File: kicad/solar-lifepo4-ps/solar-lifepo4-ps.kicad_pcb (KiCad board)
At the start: 2 copper layers, 94 x 75 mm, 56 parts, among them J1 Screw_Terminal_01x02, J2 Screw_Terminal_01x02, J3 Screw_Terminal_01x02, J4 disable-Jumper, J5 SenseVBAT, J6 SenseVSOLAR, T1 SI4435DY, T2 AO3400A, T3 AO3400A, U1 CN3722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

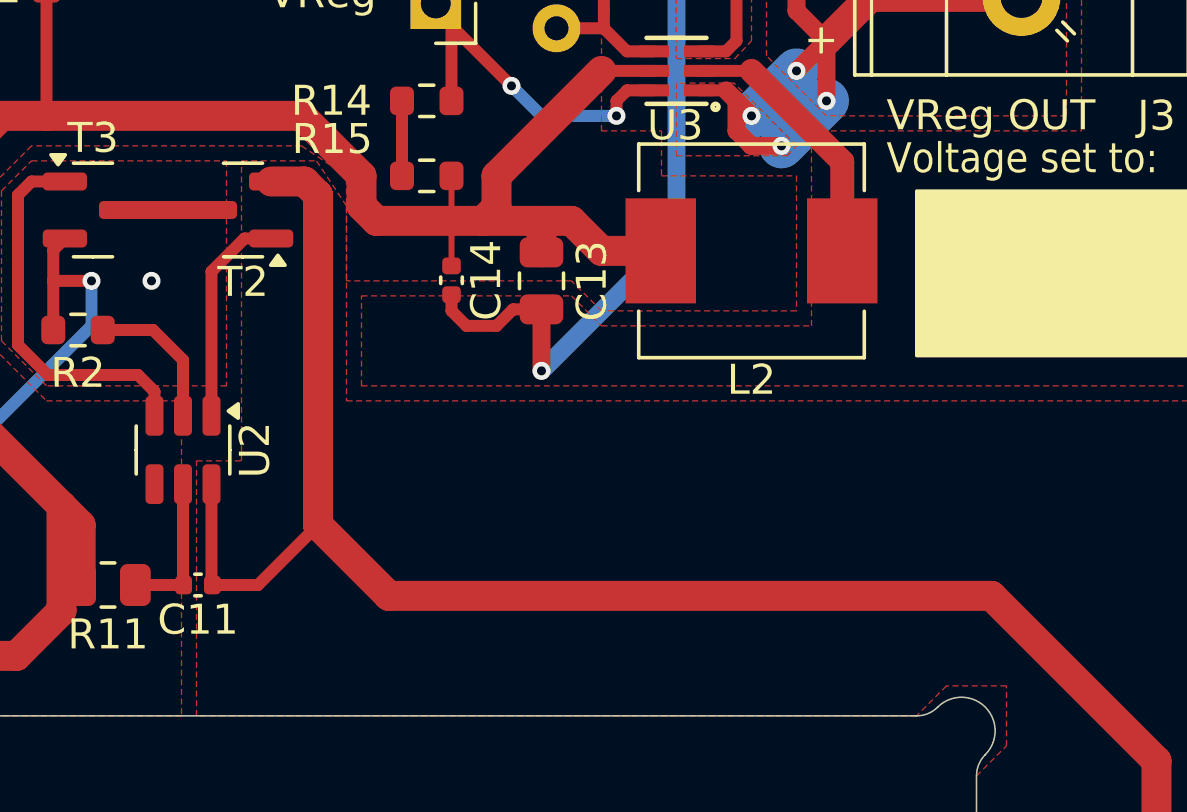
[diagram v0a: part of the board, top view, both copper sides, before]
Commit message: add pushbutton to force the battery protection circuit into "normal" mode. When a battery is inserted, but there is not and has never been enough power to actually charge, the battery protection circuit may remain in a state where the output is turned off. Shorting pins 2+6 (by pressing this button) forces the battery protection IC back into "normal" mode, with output on.
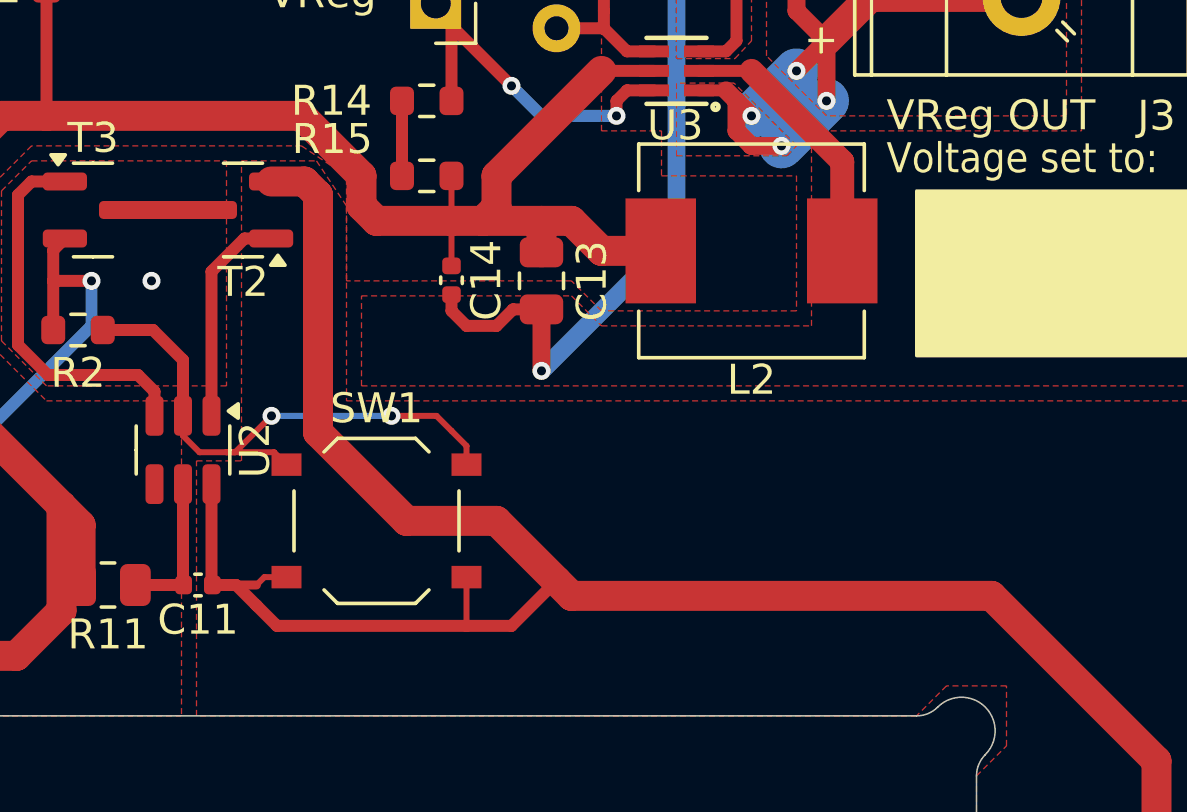
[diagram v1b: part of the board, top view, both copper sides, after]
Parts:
- added SW1: force-normal, Button_Switch_SMD:SW_Push_1P1T_XKB_TS-1187A, F.Cu at (106.5, 90.5)
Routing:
- net Net-(U2-CS): track 4.95 -> 19.0 mm, vias 0 -> 2
- net VBAT-: track 66.4 -> 76.3 mm

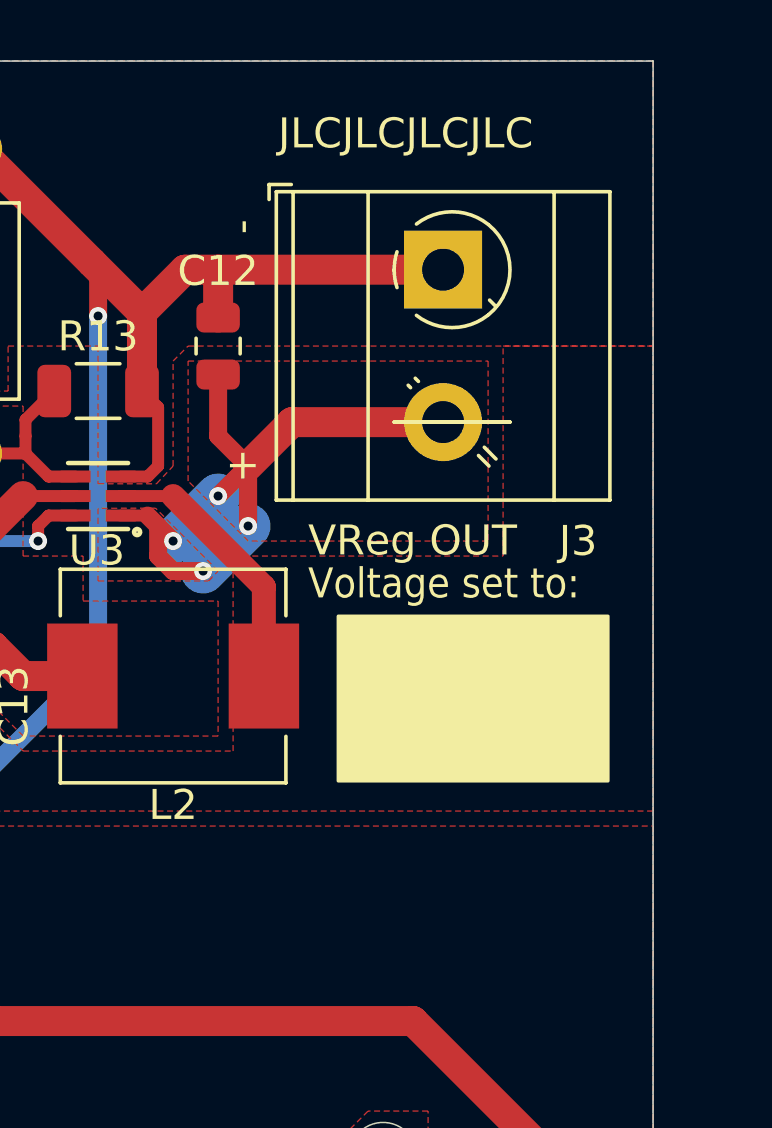
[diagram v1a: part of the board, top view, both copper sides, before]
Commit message: add more capacitors at the output of the voltage converter because as it turns out, 1x 22uF was just NOT enough. So we now have 3x 22uF instead.
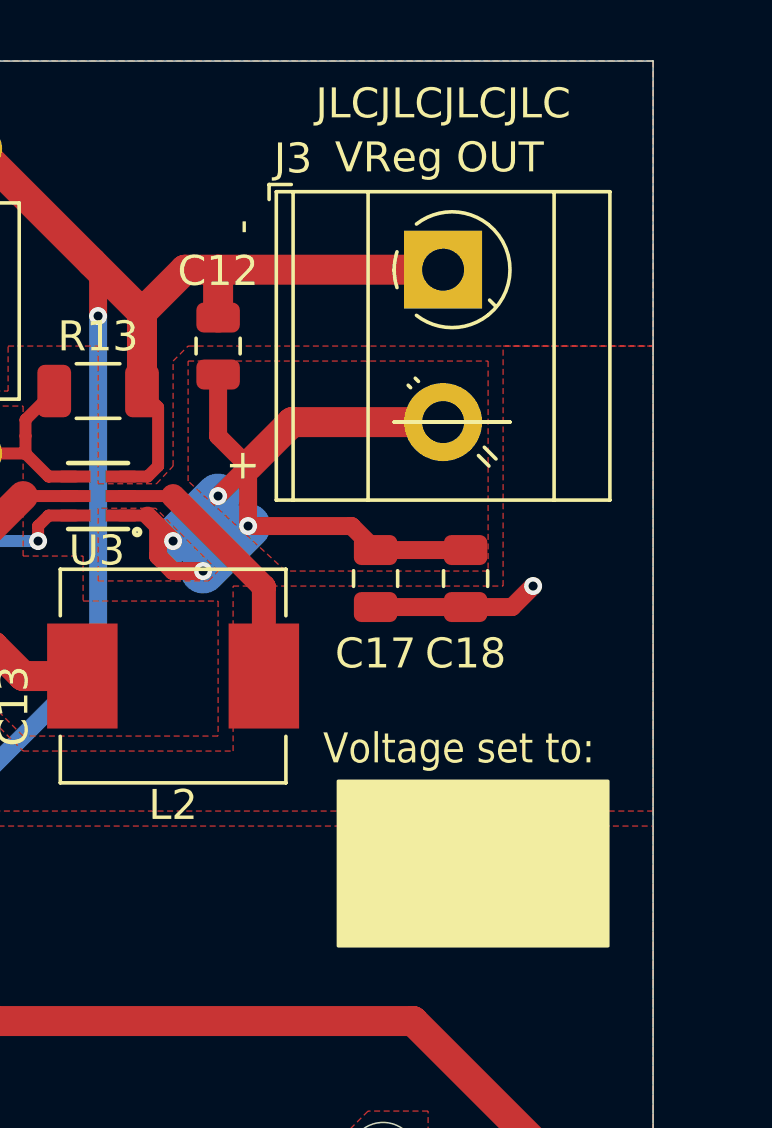
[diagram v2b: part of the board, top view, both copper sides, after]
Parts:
- added C17: 22uF, Capacitor_SMD:C_0805_2012Metric, F.Cu at (125.8, 78.2)
- added C18: 22uF, Capacitor_SMD:C_0805_2012Metric, F.Cu at (128.8, 78.2)
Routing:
- net VREGOUT: track 23.0 -> 30.6 mm
- net GND: track 245.8 -> 251.4 mm, vias 12 -> 13

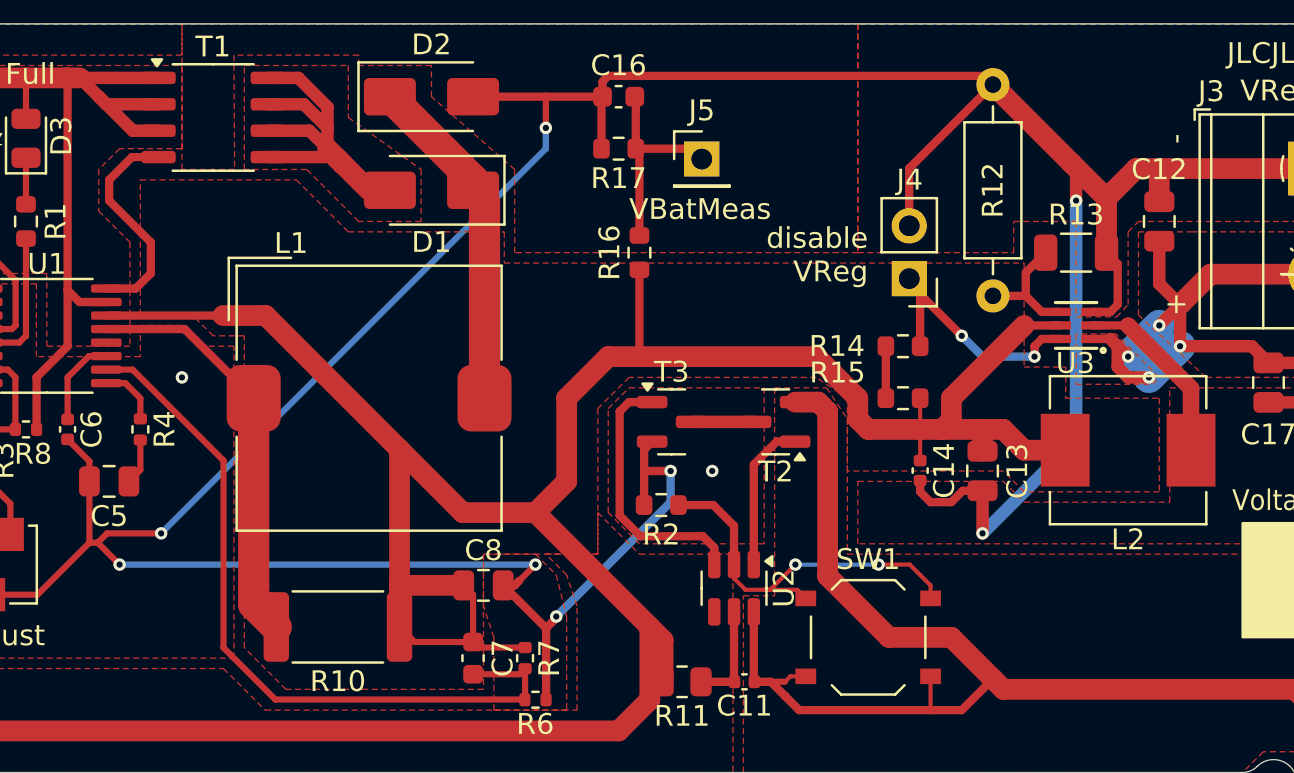
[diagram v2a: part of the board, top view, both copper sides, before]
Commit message: do not route traces below the inductor
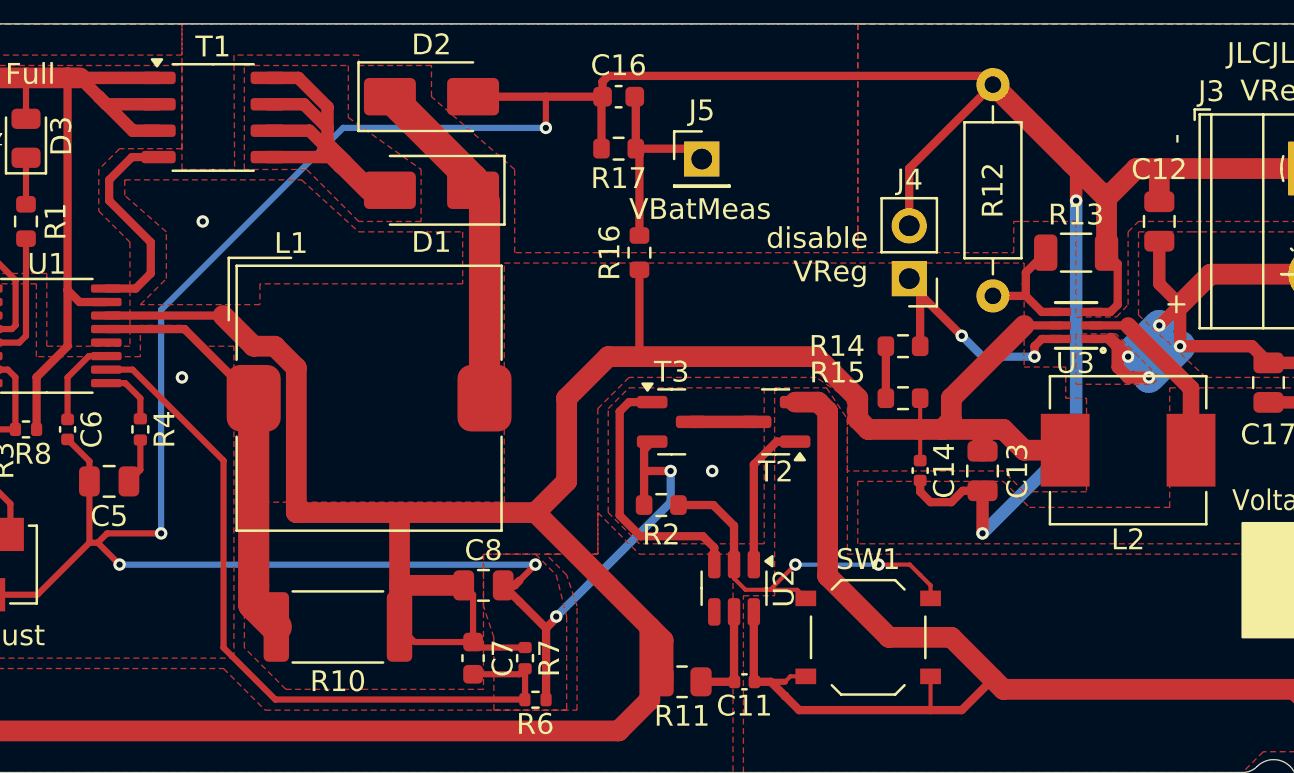
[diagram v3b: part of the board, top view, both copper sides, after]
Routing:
- net GND: track 251.4 -> 257.1 mm, vias 13 -> 14
- net VBAT+: track 189.3 -> 190.3 mm
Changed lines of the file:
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@@
+	)
+	(via
+		(at 74.5 70.5)
+		(size 0.6)
+		(drill 0.3)
+		(layers "F.Cu" "B.Cu")
+		(free yes)
+		(net 3)
 	)
 	(via
@@
 	)
 	(segment
-		(start 72.5 85.5)
-		(end 91 67)
-		(width 0.3)
-		(layer "B.Cu")
-		(net 3)
-	)
-	(segment
 		(start 70.5 87)
 		(end 90.5 87)
+		(width 0.3)
+		(layer "B.Cu")
+		(net 3)
+	)
+	(segment
+		(start 72.5 74.75)
+		(end 81.25 66)
 		(width 0.3)
 		(layer "B.Cu")
@@
 	)
 	(segment
-		(start 91 67)
-		(end 91 66)
+		(start 72.5 85.5)
+		(end 72.5 74.75)
 		(width 0.3)
 		(layer "B.Cu")
@@
 		(end 116.5 69.5)
 		(width 0.6)
+		(layer "B.Cu")
+		(net 3)
+	)
+	(segment
+		(start 81.25 66)
+		(end 91 66)
+		(width 0.3)
 		(layer "B.Cu")
 		(net 3)
@@
 	)
 	(segment
+		(start 79 84.5)
+		(end 84 84.5)
+		(width 1)
+		(layer "F.Cu")
+		(net 10)
+	)
+	(segment
 		(start 95.5 77)
 		(end 94 77)
@@
 	)
 	(segment
-		(start 87 84.5)
-		(end 90.5 84.5)
-		(width 1)
-		(layer "F.Cu")
-		(net 10)
-	)
-	(segment
 		(start 87.765 90.99)
 		(end 87.5 90.725)
@@
 		(end 87.5 88.45)
 		(width 0.3)
-		(layer "F.Cu")
-		(net 10)
-	)
-	(segment
-		(start 83.9625 81.4625)
-		(end 87 84.5)
-		(width 1)
 		(layer "F.Cu")
 		(net 10)
@@
 	)
 	(segment
+		(start 75.475 75.025)
+		(end 76.95 76.5)
+		(width 1)
+		(layer "F.Cu")
+		(net 10)
+	)
+	(segment
 		(start 46.7 112)
 		(end 46.5 112)
@@
 	)
 	(segment
-		(start 75.475 75.025)
-		(end 77.525 75.025)
-		(width 1)
-		(layer "F.Cu")
-		(net 10)
-	)
-	(segment
 		(start 94.5 95)
 		(end 54 95)
@@
 	)
 	(segment
+		(start 83.9625 84.5375)
+		(end 84 84.5)
+		(width 1)
+		(layer "F.Cu")
+		(net 10)
+	)
+	(segment
 		(start 115.925 81.55)
 		(end 115.975 81.5)
@@
 	)
 	(segment
+		(start 79 77.540812)
+		(end 79 84.5)
+		(width 1)
+		(layer "F.Cu")
+		(net 10)
+	)
+	(segment
+		(start 76.95 76.5)
+		(end 77.959188 76.5)
+		(width 1)
+		(layer "F.Cu")
+		(net 10)
+	)
+	(segment
 		(start 109 80.5)
 		(end 106.5 80.5)
@@
 	)
 	(segment
-		(start 77.525 75.025)
-		(end 83.9625 81.4625)
+		(start 84 84.5)
+		(end 90.5 84.5)
 		(width 1)
 		(layer "F.Cu")
@@
 	)
 	(segment
+		(start 83.9625 88)
+		(end 83.9625 84.5375)
+		(width 1)
+		(layer "F.Cu")
+		(net 10)
+	)
+	(segment
 		(start 95.5 72.825)
 		(end 95.5 77)
@@
 	)
 	(segment
+		(start 77.959188 76.5)
+		(end 79 77.540812)
+		(width 1)
+		(layer "F.Cu")
+		(net 10)
+	)
+	(segment
 		(start 94 77)
 		(end 92 79)
@@
 		(start 90.5 84.5)
 		(end 96 90)
-		(width 1)
-		(layer "F.Cu")
-		(net 10)
-	)
-	(segment
-		(start 83.9625 81.4625)
-		(end 83.9625 88)
 		(width 1)
 		(layer "F.Cu")
@@
 		(layer "F.Cu")
 		(hatch edge 0.5)
+		(priority 16)
+		(connect_pads
+			(clearance 0.2)
+		)
+		(min_thickness 0.25)
+		(filled_areas_thickness no)
+		(fill yes
+			(thermal_gap 0.5)
+			(thermal_bridge_width 0.5)
+		)
+		(polygon
+			(pts
+				(xy 71.5 74.5) (xy 72.75 73.25) (xy 72.75 71) (xy 70.75 69.25) (xy 70.75 68.5) (xy 79.25 68.5) (xy 82 71)
+				(xy 87 71) (xy 87 73.5) (xy 77.25 73.5) (xy 77.25 74.5)
+			)
+		)
+	)
+	(zone
+		(net 3)
+		(net_name "GND")
+		(layer "F.Cu")
+		(hatch edge 0.5)
 		(priority 15)
 		(connect_pads
@@
 		(polygon
 			(pts
-				(xy 106 86) (xy 106 83) (xy 113 83) (xy 114 84) (xy 121 84) (xy 121 78.5) (xy 130 78.5) (xy 130 70.5)
-				(xy 135 70.5) (xy 135 86)
+				(xy 106 86) (xy 106 83) (xy 113 83) (xy 114.25 84.25) (xy 121 84.25) (xy 121 78.5) (xy 130 78.5)
+				(xy 130 70.5) (xy 135 70.5) (xy 135 86)
 			)
 		)
@@
 		(polygon
 			(pts
-				(xy 71.5 68.5) (xy 79 68.5) (xy 81.5 71) (xy 89 71) (xy 89 72.5) (xy 114 72.5) (xy 114 77.5) (xy 116 77.5)
-				(xy 116 79) (xy 120.5 79) (xy 120.5 83.5) (xy 114 83.5) (xy 113 82.5) (xy 105.5 82.5) (xy 105.5 79)
-				(xy 104 78) (xy 95 78) (xy 93.5 79.5) (xy 93.5 86.5) (xy 88 86.5) (xy 88 93) (xy 78.5 93) (xy 76.5 91)
-				(xy 76.5 76) (xy 75 76) (xy 74 75) (xy 71.5 75)
+				(xy 89 84) (xy 89 72.5) (xy 114 72.5) (xy 114 77.5) (xy 116 77.5) (xy 116 79) (xy 117 79) (xy 117 83.5)
+				(xy 114 83.5) (xy 113 82.5) (xy 105.5 82.5) (xy 105.5 79) (xy 104 78) (xy 95 78) (xy 93.5 79.5)
+				(xy 93.5 86.5) (xy 88 86.5) (xy 88 93) (xy 78.5 93) (xy 76.5 91) (xy 76.5 84)
 			)
 		)
